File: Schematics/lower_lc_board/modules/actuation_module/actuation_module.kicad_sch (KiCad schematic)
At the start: 6 parts

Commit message: start layout
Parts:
- D11, D12: footprint Resistor_SMD:R_0603_1608Metric -> LED_SMD:LED_0603_1608Metric
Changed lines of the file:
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@@
 			)
 		)
-		(property "Footprint" "Resistor_SMD:R_0603_1608Metric"
+		(property "Footprint" "LED_SMD:LED_0603_1608Metric"
 			(at 91.44 96.52 0)
 			(effects
@@
 			)
 		)
-		(property "Footprint" "Resistor_SMD:R_0603_1608Metric"
+		(property "Footprint" "LED_SMD:LED_0603_1608Metric"
 			(at 91.44 81.28 0)
 			(effects

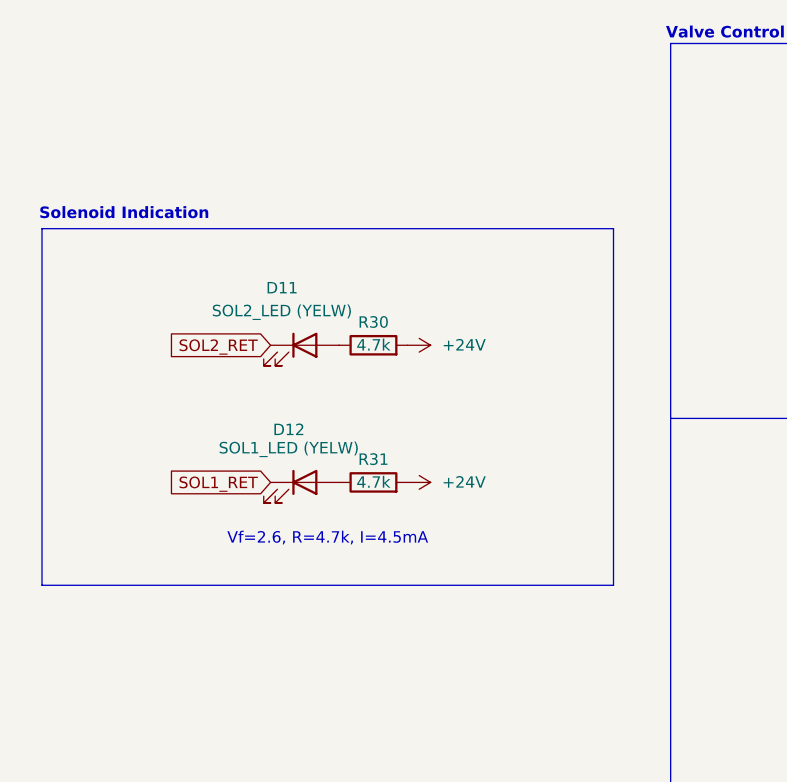
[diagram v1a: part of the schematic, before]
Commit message: layout work
#TODO
- smaller 3V3 buck, add HF cap
- finish layout
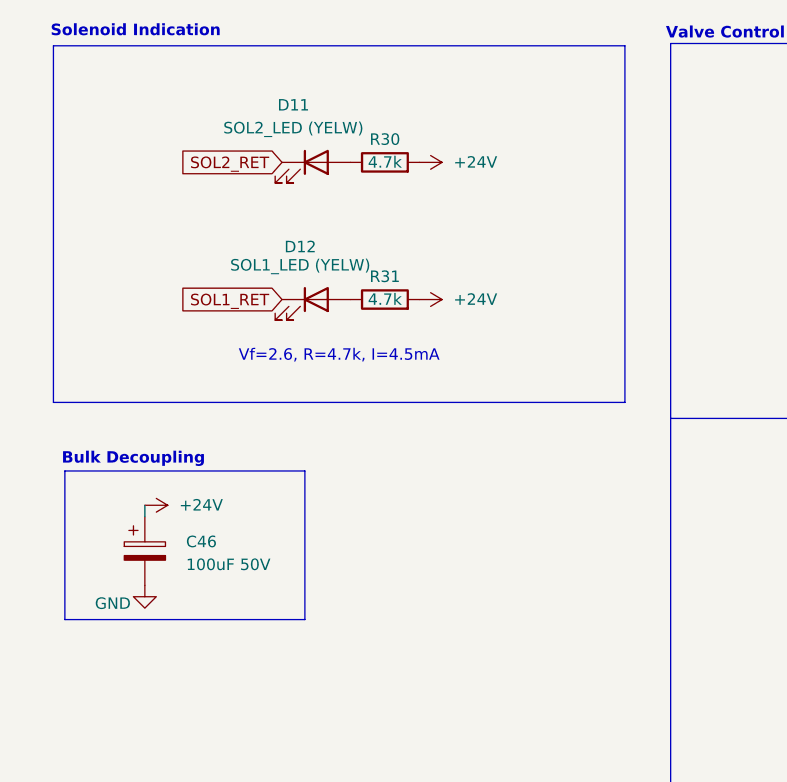
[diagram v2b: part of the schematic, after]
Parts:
- added C46: 100uF 50V, Capacitor_SMD:CP_Elec_6.3x5.9, symbol Device:C_Polarized
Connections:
- net +24V: now also C46.1
- new net GND: C46.2
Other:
- note added: "Bulk Decoupling"
- moved on the sheet: D11, D12, R30, R31

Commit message: organizational work
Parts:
- C46: value 100uF 50V -> 100uF
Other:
- moved on the sheet: C46, D11, D12, R30, R31

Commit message: more organizational work, add shared footprint, model, symbol dirs and clean up individuals
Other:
- title: Lower Board Actuation Module -> HYDRA | Actuation Circuitry
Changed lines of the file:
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@@
 	(paper "A4")
 	(title_block
-		(title "Lower Board Actuation Module")
-		(rev "B")
+		(title "HYDRA | Actuation Circuitry")
+		(rev "2")
 		(company "Queen's Rocket Engineering Team")
 		(comment 1 "Jeevan Sanchez")

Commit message: routing work
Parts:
- added Q5: 2N7002, Package_TO_SOT_SMD:SOT-23, symbol Transistor_FET:2N7002
- added R50, R51: 10k, Resistor_SMD:R_0402_1005Metric, symbol Device:R
- added R52: 10k, Resistor_SMD:R_0603_1608Metric, symbol Device:R
- added R53: 200, Resistor_SMD:R_0402_1005Metric, symbol Device:R
- added U12: SI2301CDS-T1-GE3, ul_SI2301CDS-T1-GE3:TO-236_VIS, symbol SI2301:SI2301CDS-T1-GE3
- C46: value 100uF -> 100uF
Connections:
- net +24V: now also R51.2, U12.2 (S); no longer C46.1
- net GND: now also Q5.2 (S), R52.1
- new net: Q5.3 (D), R50.1
- new net: R50.2, R51.1, U12.1 (G)
- new net: Q5.1 (G), R52.2, R53.2
- new net VSOL: C46.1, U12.3 (D)
- new net VSOL-SW: R53.1
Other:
- note added: "VSOL Switching"
- note added: "added to avoid constant power drain"
- moved on the sheet: C46, TP12

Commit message: analog routing, start 3V3 power routing
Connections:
- net +24V: no longer R30.2, R31.2
- net VSOL: now also R30.2, R31.2
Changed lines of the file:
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@@
 	)
 	(label "VSOL"
-		(at 229.87 52.07 0)
+		(at 106.68 60.96 0)
 		(fields_autoplaced yes)
 		(effects
@@
 	)
 	(label "VSOL"
-		(at 161.29 62.23 180)
+		(at 106.68 76.2 0)
 		(fields_autoplaced yes)
 		(effects
@@
 				(size 1.27 1.27)
 			)
+			(justify left bottom)
+		)
+	)
+	(label "VSOL"
+		(at 229.87 52.07 0)
+		(fields_autoplaced yes)
+		(effects
+			(font
+				(size 1.27 1.27)
+			)
+			(justify left bottom)
+		)
+	)
+	(label "VSOL"
+		(at 161.29 62.23 180)
+		(fields_autoplaced yes)
+		(effects
+			(font
+				(size 1.27 1.27)
+			)
 			(justify right bottom)
 		)
@@
 	)
 	(symbol
-		(lib_id "power:+24V")
-		(at 106.68 76.2 270)
-		(unit 1)
-		(exclude_from_sim no)
-		(in_bom yes)
-		(on_board yes)
-		(dnp no)
-		(fields_autoplaced yes)
-		(property "Reference" "#PWR081"
-			(at 102.87 76.2 0)
-			(effects
-				(font
-					(size 1.27 1.27)
-				)
-				(hide yes)
-			)
-		)
-		(property "Value" "+24V"
-			(at 110.49 76.2001 90)
-			(effects
-				(font
-					(size 1.27 1.27)
-				)
-				(justify left)
-			)
-		)
-		(property "Footprint" ""
-			(at 106.68 76.2 0)
-			(effects
-				(font
-					(size 1.27 1.27)
-				)
-				(hide yes)
-			)
-		)
-		(property "Datasheet" ""
-			(at 106.68 76.2 0)
-			(effects
-				(font
-					(size 1.27 1.27)
-				)
-				(hide yes)
-			)
-		)
-		(property "Description" "Power symbol creates a global label with name \"+24V\""
-			(at 106.68 76.2 0)
-			(effects
-				(font
-					(size 1.27 1.27)
-				)
-				(hide yes)
-			)
-		)
-		(pin "1"
-		)
-		(instances
-			(project "lower_lc_board"
-				(path "/d63798c4-e363-437e-9012-e4aff32e6642/762489dd-fdf2-4f5c-8c0c-d0a6195d3f58"
-					(reference "#PWR081")
-					(unit 1)
-				)
-			)
-		)
-	)
-	(symbol
 		(lib_id "Device:R")
 		(at 71.12 119.38 90)
@@
 					(unit 1)
 				)
-			)
-		)
-	)
-	(symbol
-		(lib_id "power:+24V")
-		(at 106.68 60.96 270)
-		(unit 1)
-		(exclude_from_sim no)
-		(in_bom yes)
-		(on_board yes)
-		(dnp no)
-		(fields_autoplaced yes)
-		(property "Reference" "#PWR076"
-			(at 102.87 60.96 0)
-			(effects
-				(font
-					(size 1.27 1.27)
-				)
-				(hide yes)
-			)
-		)
-		(property "Value" "+24V"
-			(at 110.49 60.9601 90)
-			(effects
-				(font
-					(size 1.27 1.27)
-				)
-				(justify left)
-			)
-		)
-		(property "Footprint" ""
-			(at 106.68 60.96 0)
-			(effects
-				(font
-					(size 1.27 1.27)
-				)
-				(hide yes)
-			)
-		)
-		(property "Datasheet" ""
-			(at 106.68 60.96 0)
-			(effects
-				(font
-					(size 1.27 1.27)
-				)
-				(hide yes)
-			)
-		)
-		(property "Description" "Power symbol creates a global label with name \"+24V\""
-			(at 106.68 60.96 0)
-			(effects
-				(font
-					(size 1.27 1.27)
-				)
-				(hide yes)
-			)
-		)
-		(pin "1"
-		)
-		(instances
-			(project "lower_lc_board"
-				(path "/d63798c4-e363-437e-9012-e4aff32e6642/762489dd-fdf2-4f5c-8c0c-d0a6195d3f58"
-					(reference "#PWR076")
-					(unit 1)
-				)

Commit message: more local pours and 0402 adjustments
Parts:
- R50: footprint Resistor_SMD:R_0402_1005Metric -> Resistor_SMD:R_0603_1608Metric; JLCPCB C25744 -> (none)
- R51, R53: footprint Resistor_SMD:R_0402_1005Metric -> Resistor_SMD:R_0603_1608Metric
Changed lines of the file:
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@@
 			)
 		)
-		(property "Footprint" "Resistor_SMD:R_0402_1005Metric"
+		(property "Footprint" "Resistor_SMD:R_0603_1608Metric"
 			(at 71.12 121.158 90)
 			(effects
@@
 			)
 		)
-		(property "JLCPCB" "C25744"
+		(property "JLCPCB" ""
 			(at 71.12 119.38 0)
 			(effects
@@
 			)
 		)
-		(property "Footprint" "Resistor_SMD:R_0402_1005Metric"
+		(property "Footprint" "Resistor_SMD:R_0603_1608Metric"
 			(at 93.98 108.712 90)
 			(effects
@@
 			)
 		)
-		(property "Footprint" "Resistor_SMD:R_0402_1005Metric"
+		(property "Footprint" "Resistor_SMD:R_0603_1608Metric"
 			(at 81.28 121.158 90)
 			(effects

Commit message: review of schematics and pcb
- verified all STM pins
- reviewed all circuits
- reviewed trace clearences, made sure routes are connected, etc.
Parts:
- C46: Digikey (none) -> 732-8419-1-ND; JLCPCB (none) -> 865080545012
- Q5: JLCPCB (none) -> C8545
- R30, R31: JLCPCB (none) -> C17936
- R50: JLCPCB (none) -> C25804
- R51: value 10k -> 4.7k; JLCPCB C25744 -> C23162
- U12: value SI2301CDS-T1-GE3 -> DMP4065S-7
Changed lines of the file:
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@@
+			)
+		)
+		(property "Digikey" "732-8419-1-ND"
+			(at 229.87 55.88 0)
+			(effects
+				(font
+					(size 1.27 1.27)
+				)
+				(hide yes)
+			)
+		)
+		(property "JLCPCB" "865080545012"
+			(at 229.87 55.88 0)
+			(effects
+				(font
+					(size 1.27 1.27)
+				)
+				(hide yes)
 			)
 		)
@@
 			)
 		)
+		(property "JLCPCB" "C17936"
+			(at 102.87 76.2 0)
+			(effects
+				(font
+					(size 1.27 1.27)
+				)
+				(hide yes)
+			)
+		)
 		(pin "2"
 		)
@@
 			)
 		)
-		(property "JLCPCB" ""
+		(property "JLCPCB" "C25804"
 			(at 71.12 119.38 0)
 			(effects
@@
 			)
 		)
-		(property "Value" "SI2301CDS-T1-GE3"
+		(property "Value" "DMP4065S-7"
 			(at 106.426 121.666 0)
 			(effects
@@
 			)
 		)
-		(property "Datasheet" "${KIPRJMOD}/../../Documentation/pmosfet_si2301cd_DS.pdf"
+		(property "Datasheet" "${KIPRJMOD}/../../Documentation/pmosfet_DMP4065S-7_DS.pdf"
 			(at 82.55 125.73 0)
 			(effects
@@
 			)
 		)
-		(property "Value" "10k"
+		(property "Value" "4.7k"
 			(at 83.058 119.38 90)
 			(effects
@@
 			)
 		)
-		(property "JLCPCB" "C25744"
+		(property "JLCPCB" "C23162"
 			(at 81.28 119.38 0)
 			(effects
@@
 		(property "Digikey" "311-4.70KFRCT-ND"
 			(at 102.87 60.96 90)
+			(effects
+				(font
+					(size 1.27 1.27)
+				)
+				(hide yes)
+			)
+		)
+		(property "JLCPCB" "C17936"
+			(at 102.87 60.96 0)
 			(effects
 				(font
@@
 			(at 76.2 105.41 0)
 			(effects
+				(font
+					(size 1.27 1.27)
+				)
+				(hide yes)
+			)
+		)
+		(property "JLCPCB" "C8545"
+			(at 76.2 105.41 0)
+			(effects
